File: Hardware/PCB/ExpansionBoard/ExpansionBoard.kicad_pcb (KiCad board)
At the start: 2 copper layers, 72 parts, among them IC301 STM32L452RET6, IC401 TPS7B8633QDDARQ1, IC402 MP62550DJ-LF-Z, J301 ResertConnector, J302 Conn_01x06_Socket, J401 Conn_01x02_Pin, J502 2173157-3, U201 ADXL372BCCZ-RL7, U501 FT232RL

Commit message: added Cube Project, SD Card and Tillt Switch
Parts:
- added C308: 1400n, Capacitor_SMD:C_0805_2012Metric_Pad1.18x1.45mm_HandSolder, F.Cu at (105.1, 31.5)
- added J303: MEM2061-01-188-00-A, SamacSys_Parts:MEM20610118800A, F.Cu at (116.6, 44.2)
- added R302: 0, Resistor_SMD:R_0805_2012Metric_Pad1.20x1.40mm_HandSolder, F.Cu at (105.1, 34.5)
- added R303: 0, Resistor_SMD:R_0805_2012Metric_Pad1.20x1.40mm_HandSolder, F.Cu at (105.1, 37.5)
- added S201: TM1000Q, SamacSys_Parts:TM1000Q, F.Cu at (113.4, 84.4)
- added S202: TM1000Q, SamacSys_Parts:TM1000Q, F.Cu at (131.8, 80.0)
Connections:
- IC301 pad 10: unconnected-(IC301-PC2-Pad10) -> /Accelerometer.Sheet/MISO
- IC301 pad 11: unconnected-(IC301-PC3-Pad11) -> /Accelerometer.Sheet/MOSI
- IC301 pad 29: unconnected-(IC301-PB10-Pad29) -> /MCU Sheet/CLK
- IC301 pad 5: unconnected-(IC301-PH0-OSC_IN_(PH0)-Pad5) -> /Accelerometer.Sheet/Angle_Indicator_1
- IC301 pad 6: unconnected-(IC301-PH1-OSC_OUT_(PH1)-Pad6) -> /Accelerometer.Sheet/Angle_Indicator_2
- IC301 pad 61: unconnected-(IC301-PB8-Pad61) -> /MCU Sheet/CardDetect
- IC301 pad 62: unconnected-(IC301-PB9-Pad62) -> /MCU Sheet/NSS

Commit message: finished pcb layout
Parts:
- added H401: MountingHole, MountingHole:MountingHole_2.2mm_M2, F.Cu at (81.9, 33.2)
- added H403: MountingHole, MountingHole:MountingHole_2.2mm_M2, F.Cu at (55.7, 43.2)
- added H404: MountingHole, MountingHole:MountingHole_2.2mm_M2, F.Cu at (22.1, 59.8)
- TP301, TP302, TP303, TP304, TP305, TP306, TP401, TP501, TP502, TP503, TP504, TP505, TP506, TP507, TP508, TP509, TP510: moved to B.Cu
- moved J303 83.5 mm to (33.4, 36.7), turned to 180 degrees
- moved R303 83.2 mm to (22.8, 50.1), turned to 180 degrees
- moved R302 78.7 mm to (28.1, 50.4), turned to 180 degrees
- moved S201 69.7 mm to (52.1, 51.4), turned to 90 degrees
- moved C308 65.7 mm to (39.5, 32.6), turned to 180 degrees
- moved J401 65.4 mm to (22.5, 52.9)
- moved D402 62.4 mm to (27.4, 55.5), turned to 90 degrees
- moved IC402 58.5 mm to (36.6, 53.6)
- moved JP304 58.4 mm to (68.8, 32.0)
- moved S202 57.9 mm to (77.5, 59.8), turned to 0 degrees
- moved C305 56.6 mm to (76.9, 35.2), turned to 90 degrees
- moved C307 56.5 mm to (58.6, 32.6), turned to 90 degrees
- moved C601 55.0 mm to (37.6, 46.8), turned to -90 degrees
- moved C404 54.8 mm to (32.5, 50.2)
- moved JP303 54.6 mm to (61.4, 32.0)
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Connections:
- net /MCU Sheet/CLK renamed /MCU Sheet/SD_CLK
- net /MCU Sheet/NSS renamed /MCU Sheet/SD_NSS
- net Net-(D402-A) renamed VDD
- C403 pad 2: Net-(IC402-GND) -> GND
- C404 pad 2: Net-(IC402-GND) -> GND
- IC301 pad 10: /Accelerometer.Sheet/MISO -> /MCU Sheet/SD_MISO
- IC301 pad 11: /Accelerometer.Sheet/MOSI -> /MCU Sheet/SD_MOSI
- IC402 pad 2: Net-(IC402-GND) -> GND
- J303 pad P3: /Accelerometer.Sheet/MOSI -> /MCU Sheet/SD_MOSI
- J303 pad P7: /Accelerometer.Sheet/MISO -> /MCU Sheet/SD_MISO
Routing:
- net GND: track 0.00 -> 94.9 mm, vias 0 -> 44
- net /Accelerometer.Sheet/Angle_Indicator_1: track 0.00 -> 78.8 mm, vias 0 -> 1
- net /MCU Sheet/CardDetect: track 0.00 -> 61.6 mm, vias 0 -> 2
- net +3.3V: track 0.00 -> 56.8 mm, vias 0 -> 22
- net /Accelerometer.Sheet/Angle_Indicator_2: track 0.00 -> 56.6 mm, vias 0 -> 3
- net /MCU Sheet/SD_NSS: track 0.00 -> 52.4 mm, vias 0 -> 2
- net /MCU Sheet/SD_MOSI: track 0.00 -> 43.4 mm, vias 0 -> 2
- net /MCU Sheet/SD_MISO: track 0.00 -> 37.9 mm, vias 0 -> 2
- net /Airspeed Sheet/SDA: track 0.00 -> 36.3 mm, vias 0 -> 2
- net /MCU Sheet/SD_CLK: track 0.00 -> 34.0 mm, vias 0 -> 2
- net /Airspeed Sheet/SCL: track 0.00 -> 33.8 mm, vias 0 -> 2
- net /MCU Sheet/~{nRST}: track 0.00 -> 33.6 mm, vias 0 -> 2
- net /Accelerometer.Sheet/INT_2: track 0.00 -> 24.4 mm
- net /MCU Sheet/SWCLK: track 0.00 -> 22.8 mm, vias 0 -> 1
- net /MCU Sheet/MCU_TX: track 0.00 -> 22.6 mm, vias 0 -> 4
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- added copper zone on In2.Cu, net +3.3V
- added copper zone on In2.Cu, net +5V
- added copper zone on In1.Cu, net GND
- added copper zone on In2.Cu, net VDD
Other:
- board outline added: 65.5 x 32 mm
- copper layers 2 -> 4

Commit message: finsihed filling
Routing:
- net GND: track 94.9 -> 88.6 mm, vias 44 -> 90
- added copper zone on B.Cu, net GND
- added copper zone on F.Cu, net GND
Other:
- board text added: "+"
- board text added: "-"

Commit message: finsihed pcb
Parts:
- moved C308 0.94 mm to (38.5, 32.6)
- moved C303 0.08 mm to (65.2, 32.0)
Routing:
- net GND: track 88.6 -> 87.5 mm, vias 90 -> 239
- net +3.3V: track 56.8 -> 57.7 mm, vias 22 -> 23
- net VDD: vias 4 -> 3

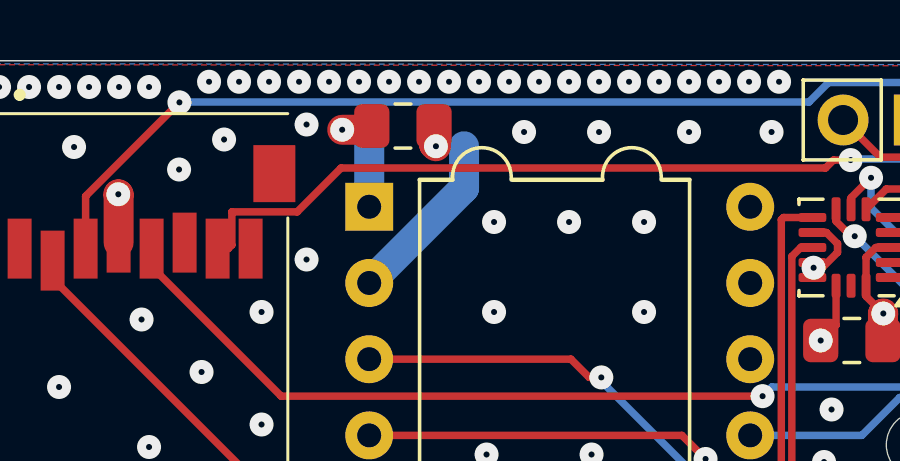
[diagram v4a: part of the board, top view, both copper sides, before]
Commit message: removed error in drc
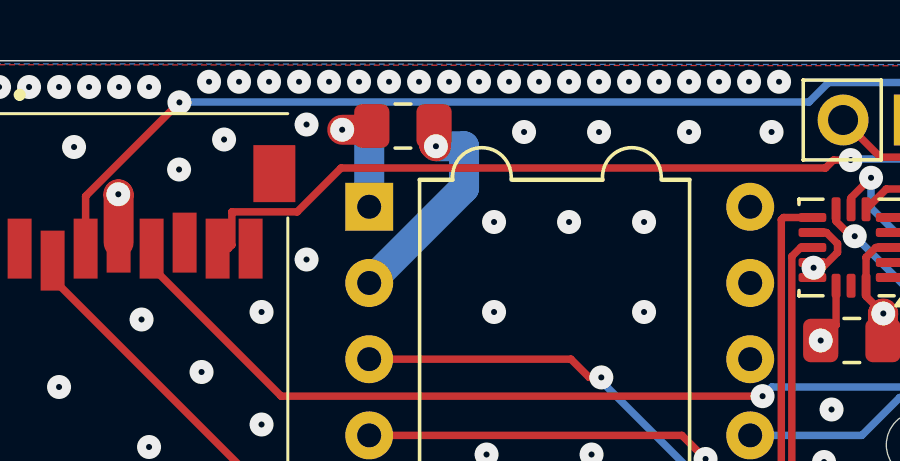
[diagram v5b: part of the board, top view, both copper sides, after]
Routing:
- net +3.3V: track 57.7 -> 58.7 mm
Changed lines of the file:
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@@
+	)
+	(segment
+		(start 40.55 33.285)
+		(end 39.6125 33.285)
+		(width 1)
+		(layer "B.Cu")
+		(net 6)
 	)
 	(segment
